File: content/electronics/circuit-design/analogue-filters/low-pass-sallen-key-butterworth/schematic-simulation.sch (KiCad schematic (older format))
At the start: 8 parts, among them U1 AD8051

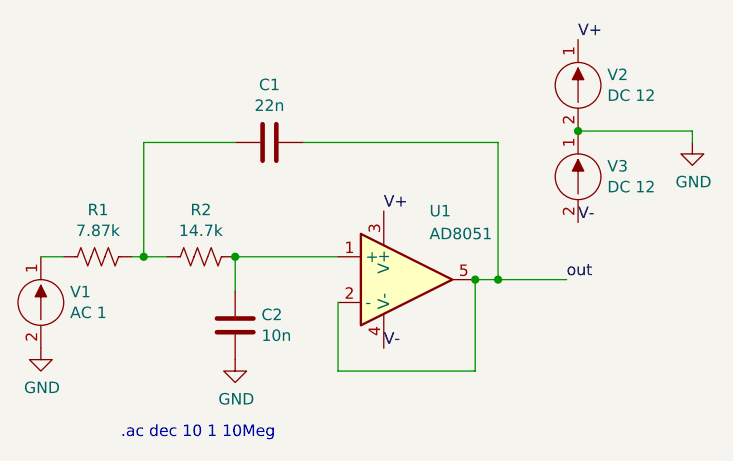
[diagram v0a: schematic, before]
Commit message: Added a Bessel optimized low-pass Sallen-Key filter simulation schematic and added the results of the comparison plots.
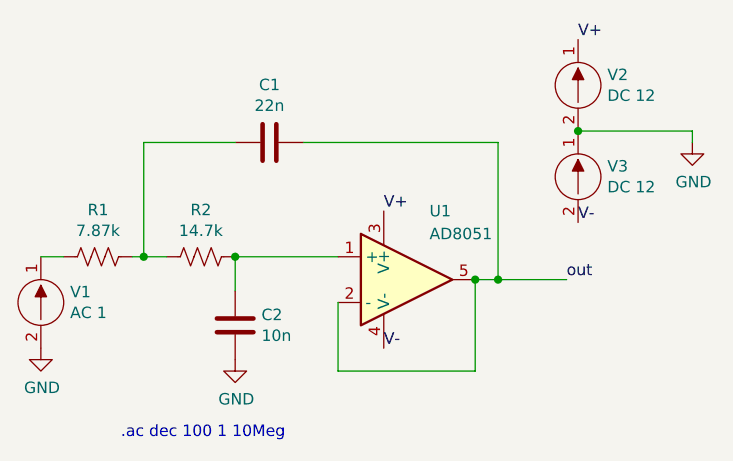
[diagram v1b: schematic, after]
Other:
- note added: ".ac dec 100 1 10Meg"
- note removed: ".ac dec 10 1 10Meg"
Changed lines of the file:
@@
 V-
 Text Notes 4150 4450 0    50   ~ 0
-.ac dec 10 1 10Meg
+.ac dec 100 1 10Meg
 $EndSCHEMATC
